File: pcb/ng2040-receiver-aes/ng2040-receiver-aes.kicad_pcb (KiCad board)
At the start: 2 copper layers, 30 x 31.5 mm, 18 parts, among them J1 DB15_F, SW1 OPTS, U1 RP2040-Zero, U2 NRF24L01_Breakout

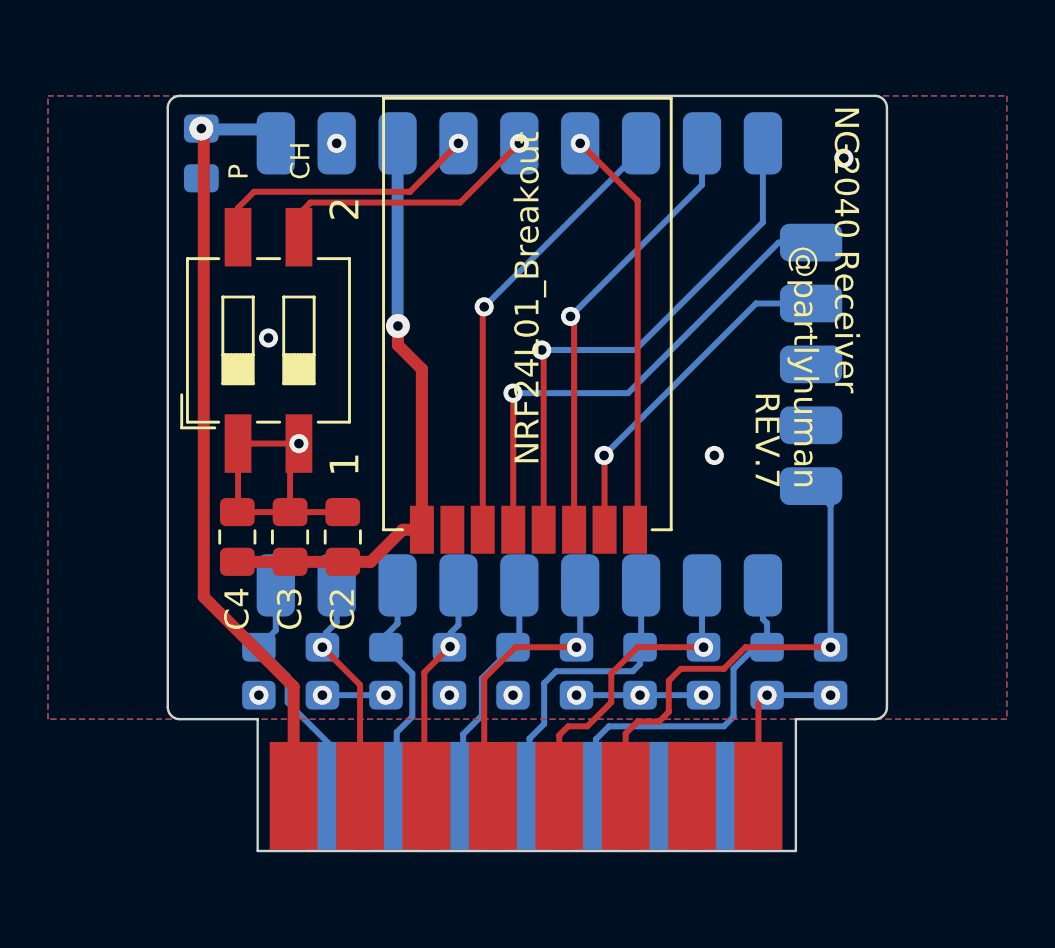
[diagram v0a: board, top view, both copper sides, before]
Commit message: AES give more padding distance to allow for plastic collar
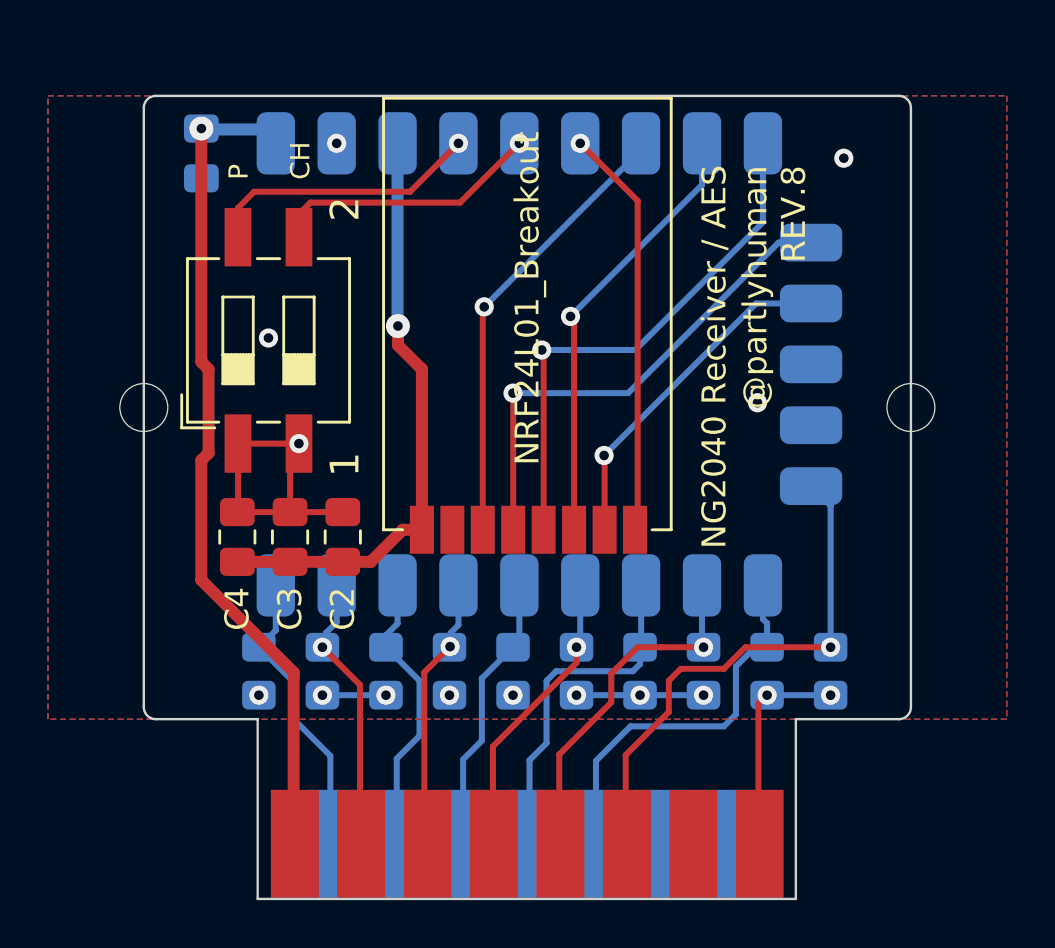
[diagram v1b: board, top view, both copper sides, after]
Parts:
- added H1: MountingHole_2mm, MountingHole:MountingHole_2mm, F.Cu at (84.0, 70.0)
- added H2: MountingHole_2mm, MountingHole:MountingHole_2mm, F.Cu at (116.0, 70.0)
- moved J1 2.00 mm to (100.2, 88.2)
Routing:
- net /DL: track 9.71 -> 11.8 mm
- net GND: track 27.8 -> 29.6 mm
- net /DD: track 9.68 -> 11.5 mm
- net /DU: track 10.3 -> 12.1 mm
- net /DR: track 9.44 -> 11.2 mm
- net /BC: track 12.6 -> 14.4 mm
- net /BA: track 9.75 -> 11.6 mm
- net /VCC: track 33.2 -> 34.8 mm
- net /BD: track 13.4 -> 14.7 mm
- net /STA: track 14.9 -> 16.2 mm
- net /SEL: track 20.5 -> 21.7 mm
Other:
- board size 30 x 31.5 mm -> 32 x 33.5 mm

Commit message: AES shave down
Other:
- board size 32 x 33.5 mm -> 32 x 33.4 mm
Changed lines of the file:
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@@
 	(generator_version "9.0")
 	(general
-		(thickness 1.6)
+		(thickness 1.2)
 		(legacy_teardrops no)
 	)
@@
 			(layer "dielectric 1"
 				(type "core")
-				(thickness 1.51)
+				(thickness 1.11)
 				(material "FR4")
 				(epsilon_r 4.5)
@@
 	)
 	(gr_line
-		(start 84 82.5)
+		(start 84 83.5)
 		(end 84 69)
 		(stroke
@@
 	)
 	(gr_line
-		(start 116 82.5)
+		(start 116 83.5)
 		(end 116 69)
 		(stroke
@@
 	)
 	(gr_arc
-		(start 84.5 83)
-		(mid 84.146447 82.853553)
-		(end 84 82.5)
+		(start 115.5 57)
+		(mid 115.853553 57.146447)
+		(end 116 57.5)
 		(stroke
 			(width 0.1)
@@
 	)
 	(gr_arc
-		(start 116 82.5)
-		(mid 115.853553 82.853553)
-		(end 115.5 83)
+		(start 116 83.5)
+		(mid 115.853553 83.853553)
+		(end 115.5 84)
 		(stroke
 			(width 0.1)
@@
 		(layer "Edge.Cuts")
 	)
-	(gr_arc
-		(start 115.5 57)
-		(mid 115.853553 57.146447)
-		(end 116 57.5)
+	(gr_line
+		(start 115.5 84)
+		(end 110.7 84)
 		(stroke
 			(width 0.1)
@@
 	)
 	(gr_line
-		(start 88.75 83)
-		(end 88.75 90.5)
+		(start 84.5 84)
+		(end 89.3 84)
 		(stroke
 			(width 0.1)
@@
 	)
 	(gr_line
-		(start 84 69)
-		(end 84 57.5)
+		(start 89.3 84)
+		(end 89.3 90.4)
 		(stroke
 			(width 0.1)
@@
 	)
 	(gr_line
-		(start 88.75 90.5)
-		(end 111.2 90.5)
+		(start 84 69)
+		(end 84 57.5)
 		(stroke
 			(width 0.1)
@@
 	)
 	(gr_line
-		(start 111.2 90.5)
-		(end 111.2 83)
+		(start 89.3 90.4)
+		(end 110.7 90.4)
 		(stroke
 			(width 0.1)
@@
 	)
 	(gr_line
-		(start 115.5 83)
-		(end 111.2 83)
+		(start 110.7 90.4)
+		(end 110.7 84)
 		(stroke
 			(width 0.1)
@@
 		(layer "Edge.Cuts")
 	)
-	(gr_line
-		(start 84.5 83)
-		(end 88.75 83)
+	(gr_arc
+		(start 84.5 84)
+		(mid 84.146447 83.853553)
+		(end 84 83.5)
 		(stroke
 			(width 0.1)
@@
 	)
 	(gr_text "2"
-		(at 93.1 61.2 90)
+		(at 93.1 61.9 90)
 		(layer "F.SilkS")
 		(effects
@@
 	)
 	(gr_text "1"
-		(at 93.1 72.9 90)
+		(at 93.1 72.2 90)
 		(layer "F.SilkS")
 		(effects
@@
 	)
 	(gr_text "P\n\nCH"
-		(at 91 60.5 90)
+		(at 91 61.2 90)
 		(layer "F.SilkS")
 		(effects
@@
 	(segment
 		(start 86.4 58.3625)
-		(end 86.4 68.1)
-		(width 0.5)
-		(layer "F.Cu")
-		(net 2)
-	)
-	(segment
-		(start 86.4 68.1)
-		(end 86.7 68.4)
-		(width 0.5)
-		(layer "F.Cu")
-		(net 2)
-	)
-	(segment
-		(start 86.4 77.2)
-		(end 90.25 81.05)
-		(width 0.5)
-		(layer "F.Cu")
-		(net 2)
-	)
-	(segment
-		(start 86.4 72.2)
-		(end 86.4 77.2)
-		(width 0.5)
-		(layer "F.Cu")
-		(net 2)
-	)
-	(segment
-		(start 86.7 71.9)
-		(end 86.4 72.2)
+		(end 86.4 77.8)
 		(width 0.5)
 		(layer "F.Cu")
@@
 	)
 	(segment
-		(start 86.7 68.4)
-		(end 86.7 71.9)
+		(start 86.4 77.8)
+		(end 90.25 81.65)
 		(width 0.5)
 		(layer "F.Cu")
@@
 	)
 	(segment
-		(start 90.25 81.05)
+		(start 90.25 81.65)
 		(end 90.25 88)
 		(width 0.5)
@@
 		(polygon
 			(pts
-				(xy 120 83) (xy 80 83) (xy 80 57) (xy 120 57)
+				(xy 120 84) (xy 80 84) (xy 80 57) (xy 120 57)
 			)
 		)

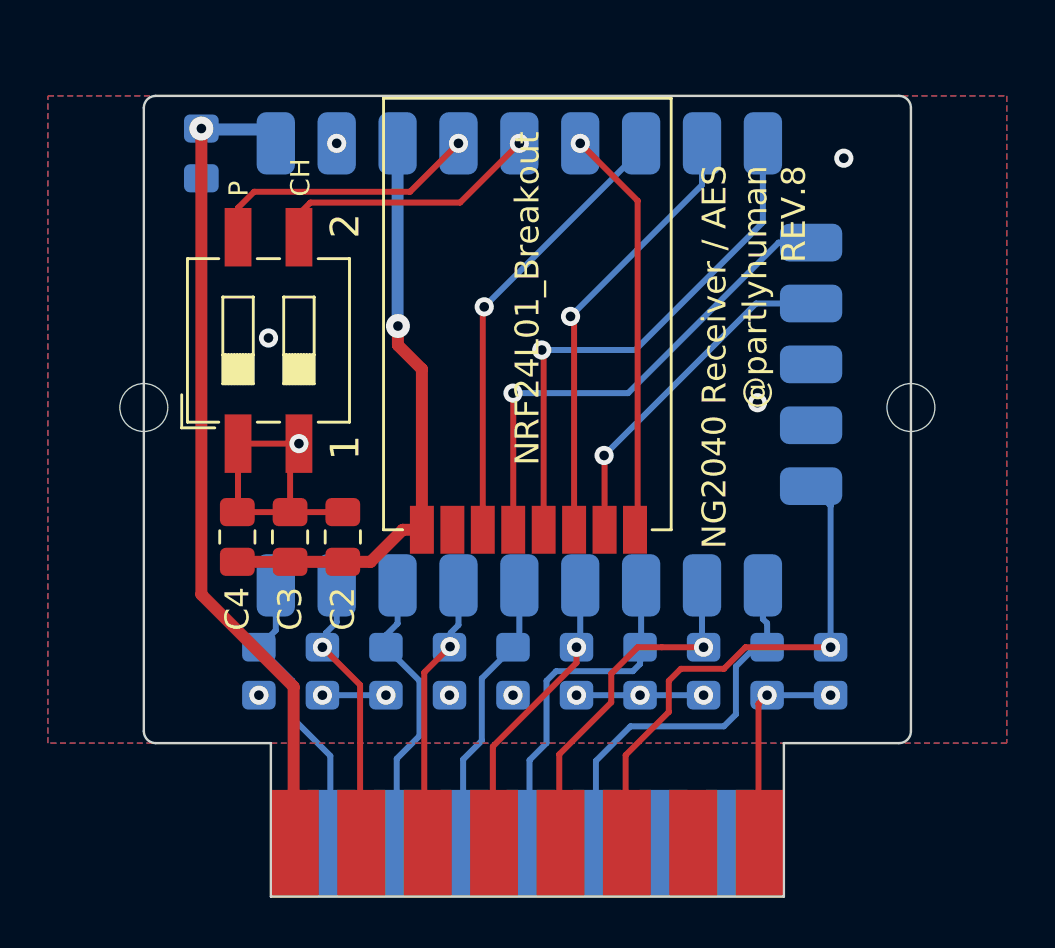
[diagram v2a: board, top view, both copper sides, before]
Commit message: AES removeall extra depth
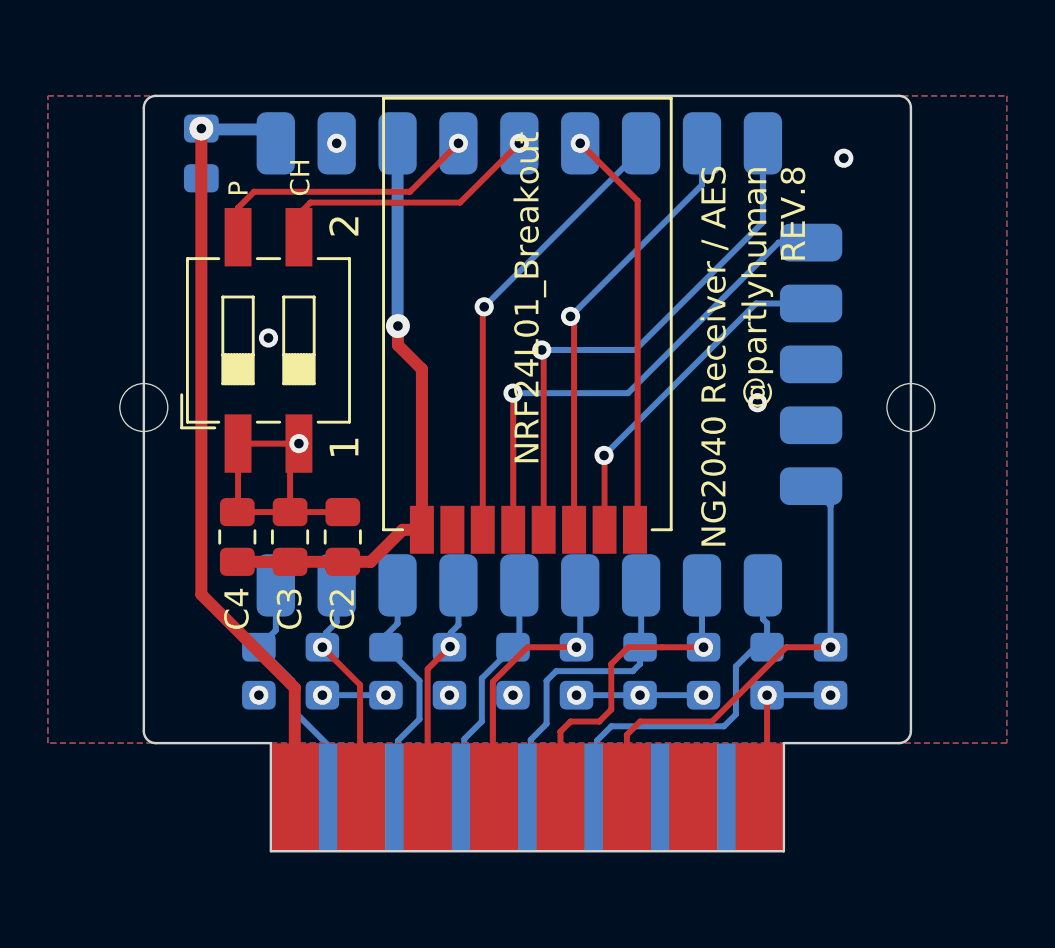
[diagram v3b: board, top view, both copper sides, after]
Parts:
- moved J1 1.94 mm to (100.2, 86.3)
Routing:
- net /SEL: track 21.7 -> 19.7 mm
- net /DR: track 11.2 -> 9.37 mm
- net /BA: track 11.6 -> 9.79 mm
- net GND: track 29.6 -> 27.8 mm
- net /DL: track 11.8 -> 9.99 mm
- net /BC: track 14.4 -> 12.6 mm
- net /VCC: track 34.6 -> 32.9 mm
- net /DU: track 12.1 -> 10.4 mm
- net /DD: track 11.5 -> 9.76 mm
- net /STA: track 16.2 -> 14.9 mm
- net /BD: track 14.7 -> 13.9 mm
- net /BB: track 12.1 -> 11.6 mm
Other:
- board size 32 x 33.4 mm -> 32 x 31.5 mm
